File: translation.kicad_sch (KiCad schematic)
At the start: 12 parts, among them Q1 DMG1012UW-7, Q2 DMG1013UW-7, Q3 DMG1012UW-7, U4 FXLA108BQX

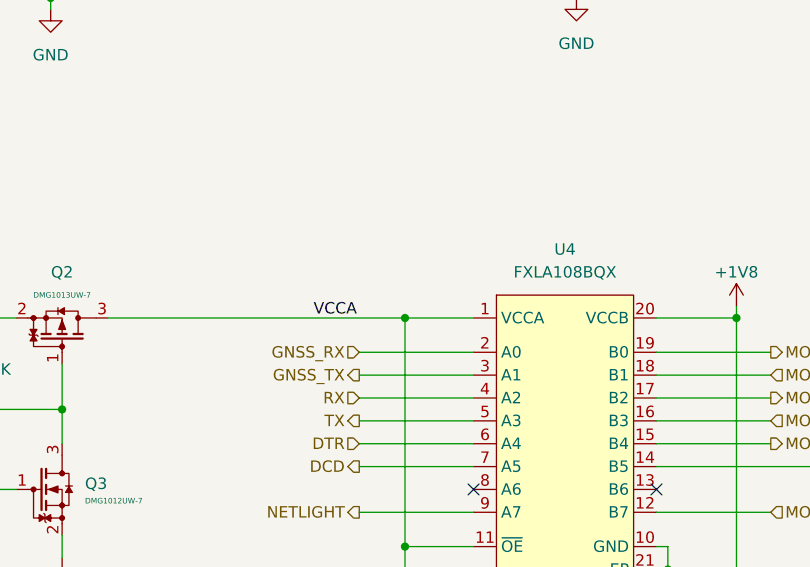
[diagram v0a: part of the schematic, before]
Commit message: Add TP for VDDA
Change board color to blue
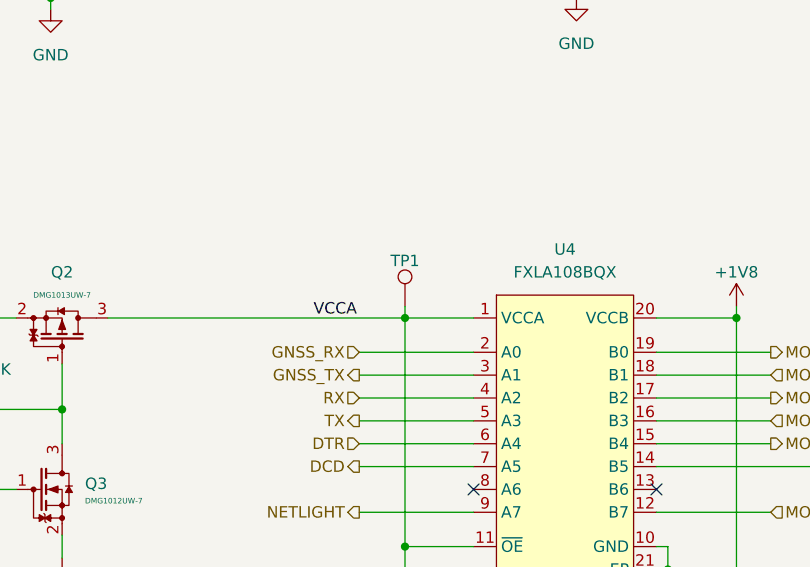
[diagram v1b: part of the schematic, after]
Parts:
- added TP1: ~, N_NonPart:TestPoint_1mm, symbol N_NonPart:TestPoint_1mm
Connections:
- net VCCA: now also TP1.1
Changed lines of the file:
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@@
+    (stroke (width 0) (type default))
+  )
+  (wire (pts (xy 120.65 91.44) (xy 120.65 92.71))
     (stroke (width 0) (type default))
   )
@@
         )
       )
+    )
+  )
+  (symbol (lib_id "N_NonPart:TestPoint_1mm") (at 120.65 91.44 0) (unit 1)
+    (in_bom no) (on_board yes) (dnp no)
+    (property "Reference" "TP1" (at 120.65 86.36 0)
+      (effects (font (size 1.27 1.27)))
+    )
+    (property "Value" "~" (at 120.65 91.44 0)
+      (effects (font (size 1.27 1.27)))
+    )
+    (property "Footprint" "N_NonPart:TestPoint_1mm" (at 120.65 91.44 0)
+      (effects (font (size 1.27 1.27)) hide)
+    )
+    (property "Datasheet" "" (at 120.65 91.44 0)
+      (effects (font (size 1.27 1.27)) hide)
+    )
+    (pin "1")
+    (instances
+      (project "Winglet-BG95"
+        (path "/332623d6-c22a-48da-966b-0d541566aa2d/8e359055-7cfc-4b97-a20a-120bbd795961"
+          (reference "TP1") (unit 1)
+        )
+        (path "/332623d6-c22a-48da-966b-0d541566aa2d/8db25416-284f-4798-9948-d4496aafbc9d"
+          (reference "TP2") (unit 1)
+        )
+      )

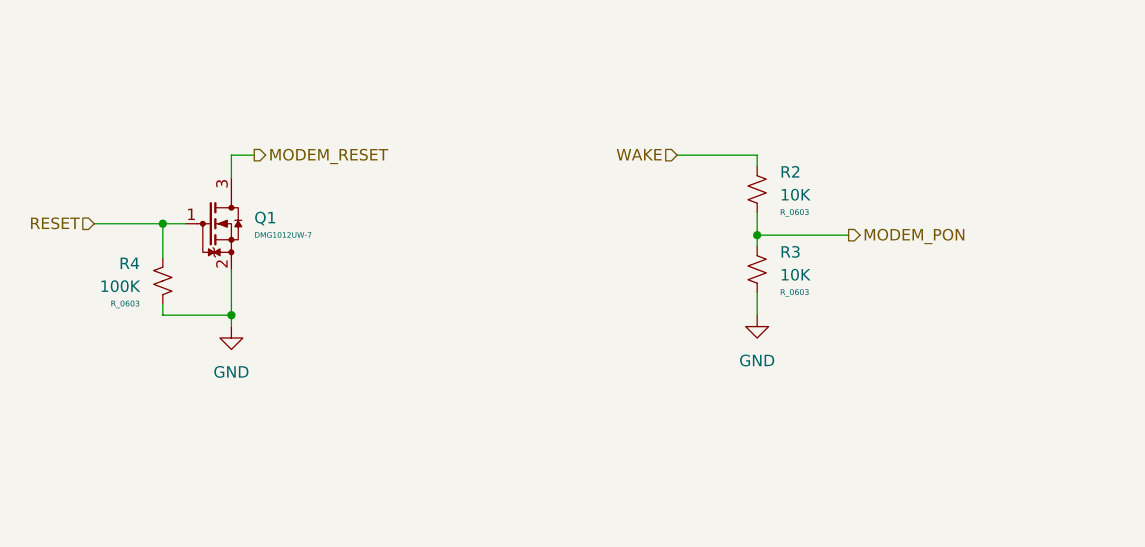
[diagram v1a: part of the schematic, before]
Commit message: Remove PON_TRIG key, add PWRKEY control.
Remove USIM options on PCIE interface.
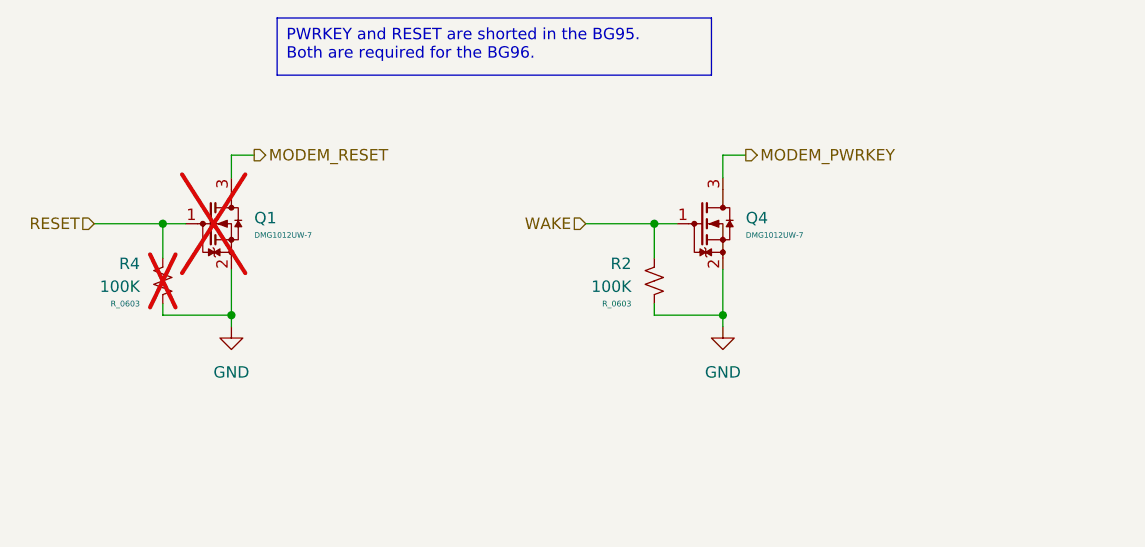
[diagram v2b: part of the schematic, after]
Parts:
- removed R3: 10K, R_Resistor:R_0603, symbol R_Resistor:R_0603
- added Q4: DMG1012UW-7, U_IC:SC70-3, symbol Q_MOSFET:DMG1012UW-7
- Q1, R4: now not fitted
- R2: value 10K -> 100K
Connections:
- net MODEM_PON is gone; now on net GND: R2.2
- net GND: now also Q4.2 (S)
- net WAKE: now also Q4.1 (G)
- new net MODEM_PWRKEY: Q4.3 (D)

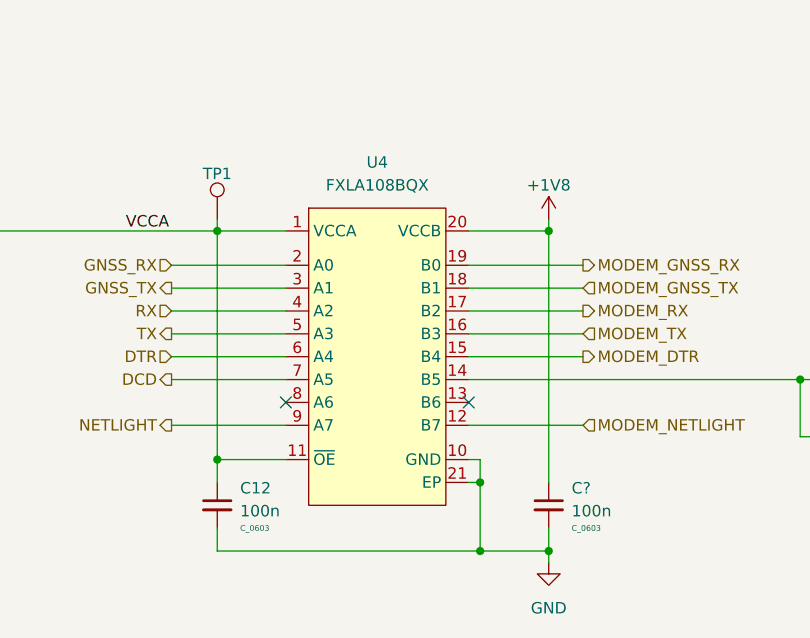
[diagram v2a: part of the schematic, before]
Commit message: Added tooling holes
Updated the readme
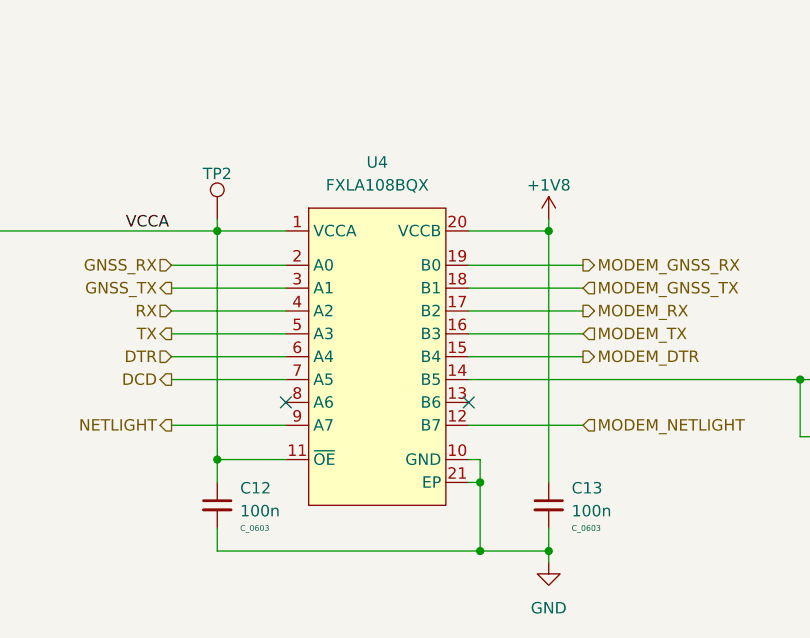
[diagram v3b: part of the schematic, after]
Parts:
- gave numbers to parts that had none: 1
- renumbered TP1 to TP2

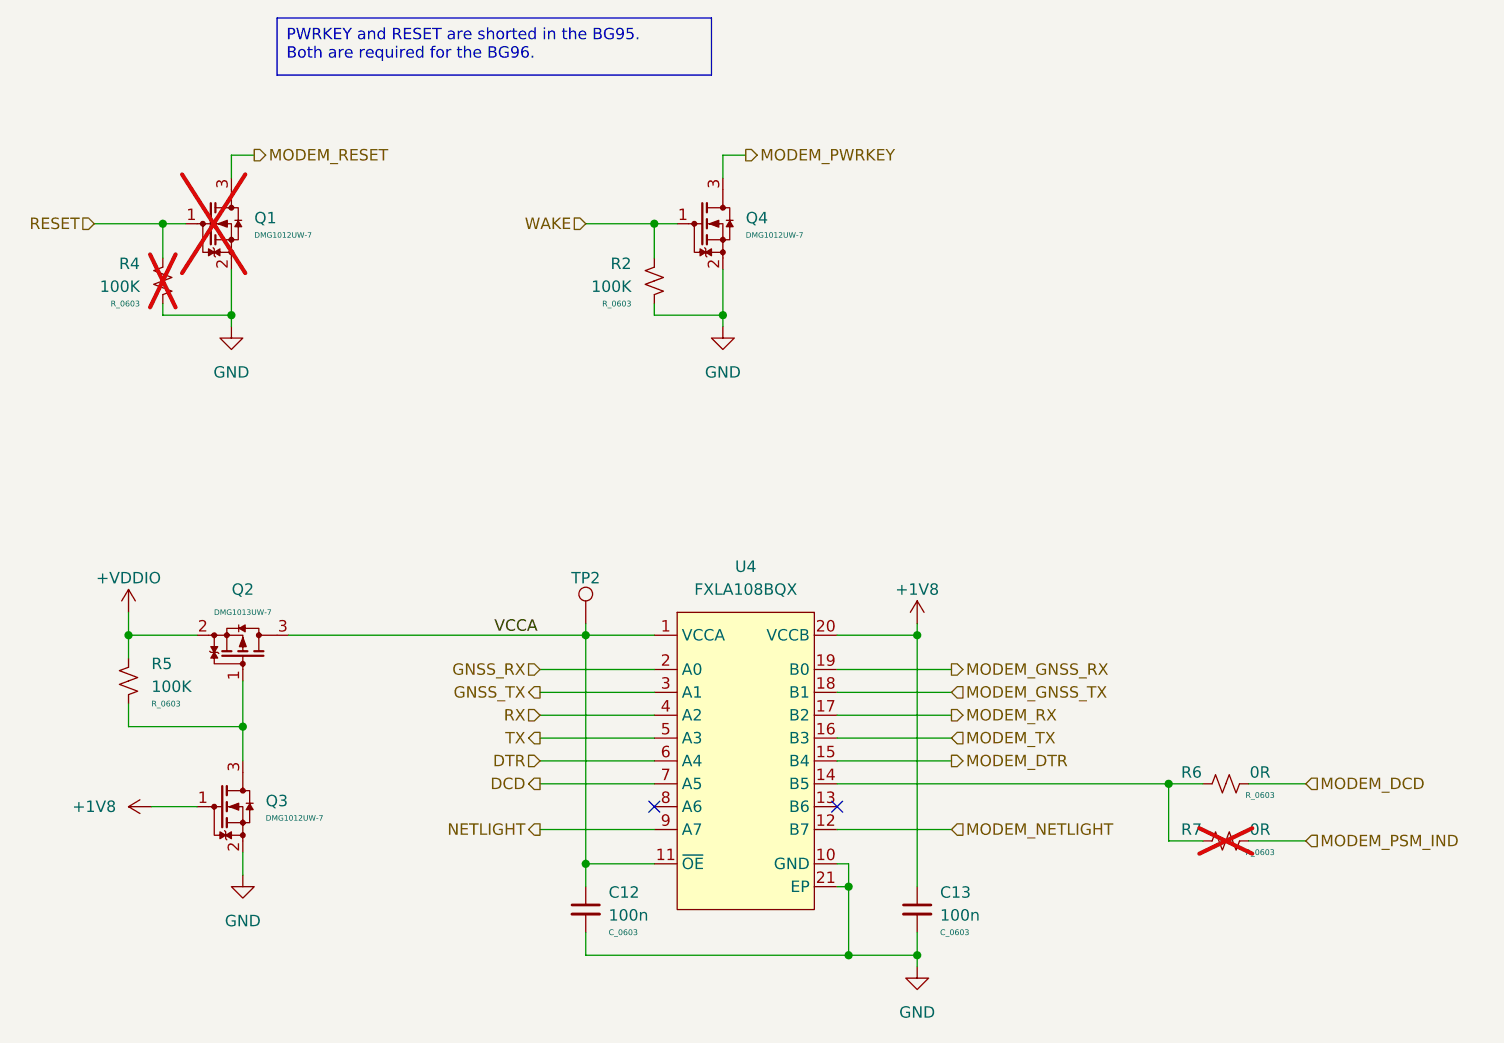
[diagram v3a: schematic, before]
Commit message: Implement fixes
Closes #2
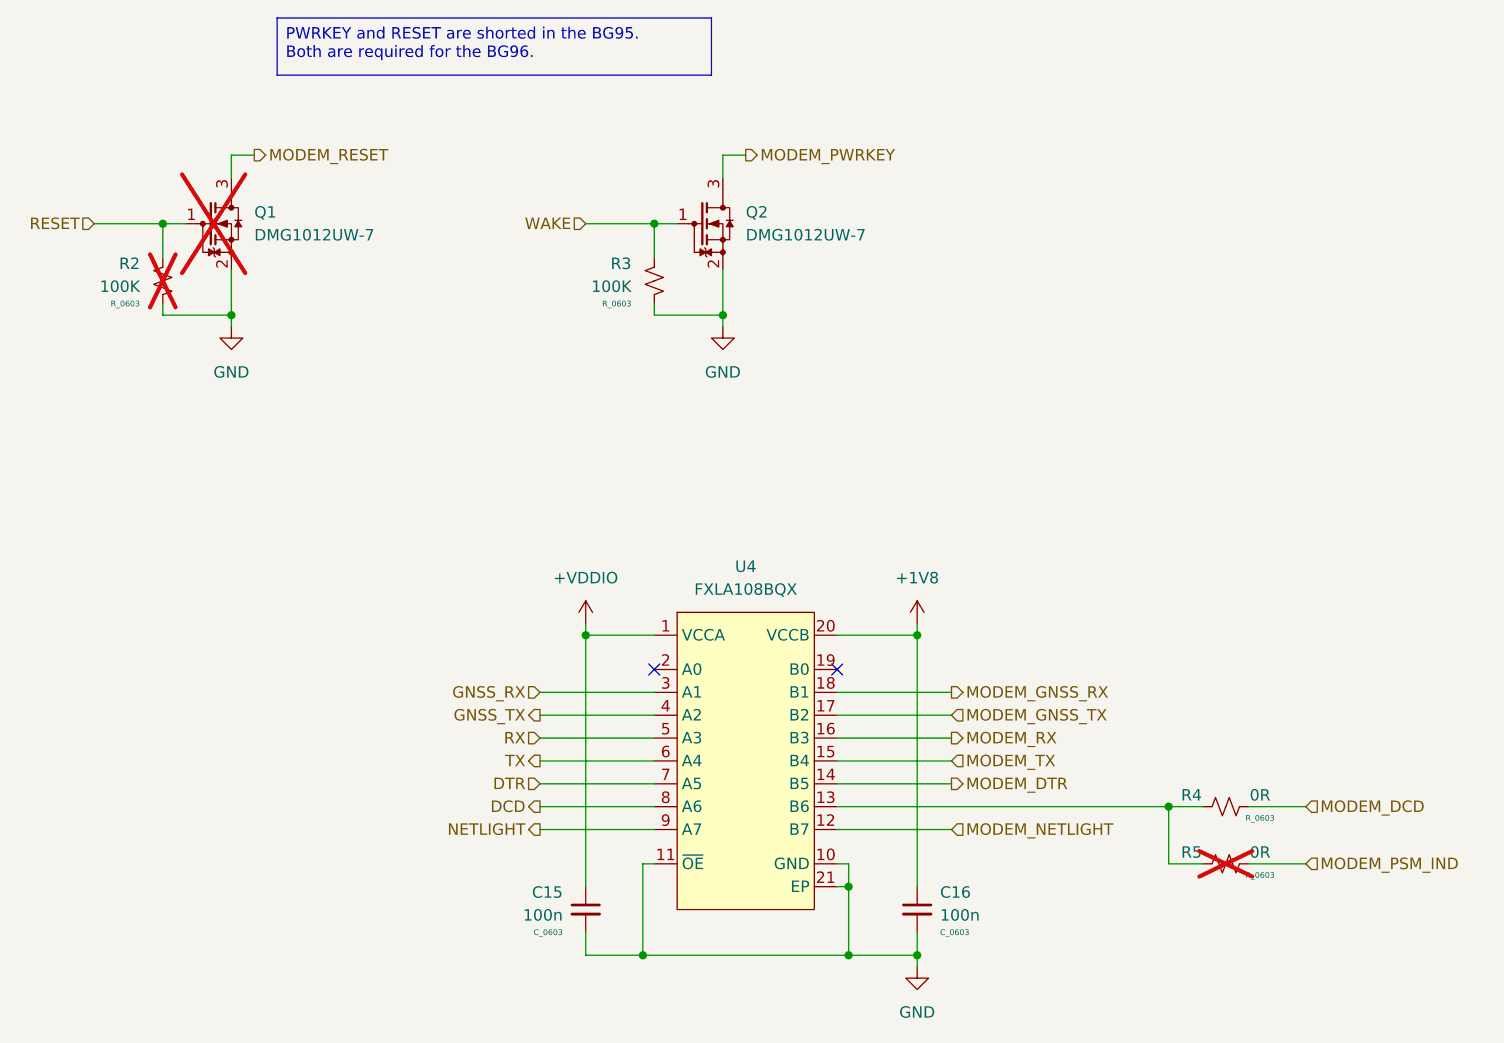
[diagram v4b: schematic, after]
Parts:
- removed Q2: DMG1013UW-7, U_IC:SC70-3, symbol Q_MOSFET:DMG1013UW-7
- removed Q3: DMG1012UW-7, U_IC:SC70-3, symbol Q_MOSFET:DMG1012UW-7
- removed R5: 100K, R_Resistor:R_0603, symbol R_Resistor:R_0603
- removed TP2: ~, N_NonPart:TestPoint_1mm, symbol N_NonPart:TestPoint_1mm
- renumbered C12 to C15, C13 to C16, Q4 to Q2, R4 to R2, R2 to R3, R6 to R4, R7 to R5
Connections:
- net +VDDIO: now also C15.1, U4.1 (VCCA)
- net DCD: now also U4.8 (A6); no longer U4.7 (A5)
- net DTR: now also U4.7 (A5); no longer U4.6 (A4)
- net GND: now also U4.11 (~{OE})
- net GNSS_RX: now also U4.3 (A1); no longer U4.2 (A0)
- net GNSS_TX: now also U4.4 (A2); no longer U4.3 (A1)
- net MODEM_DTR: now also U4.14 (B5); no longer U4.15 (B4)
- net MODEM_GNSS_RX: now also U4.18 (B1); no longer U4.19 (B0)
- net MODEM_GNSS_TX: now also U4.17 (B2); no longer U4.18 (B1)
- net MODEM_RX: now also U4.16 (B3); no longer U4.17 (B2)
- net MODEM_TX: now also U4.15 (B4); no longer U4.16 (B3)
- net RX: now also U4.5 (A3); no longer U4.4 (A2)
- net TX: now also U4.6 (A4); no longer U4.5 (A3)
- net at R4.2, R5.2: now also U4.13 (B6); no longer U4.14 (B5)
- removed net VCCA: C15.1, U4.1 (VCCA), U4.11 (~{OE})
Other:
- company: (none) -> TL Embedded
- title: (none) -> Winglet BG95
- moved on the sheet: R4, R5

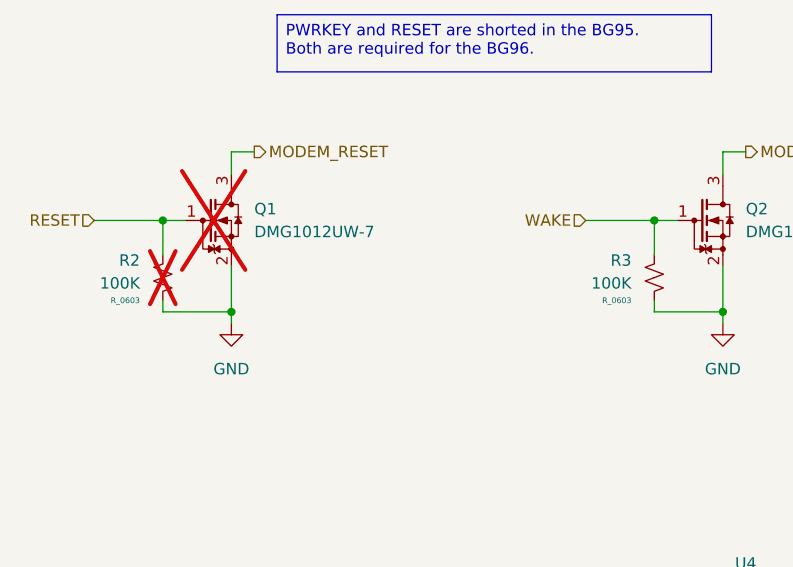
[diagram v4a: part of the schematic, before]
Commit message: Move to NSIM-16-B sim card holder for easier sourcing
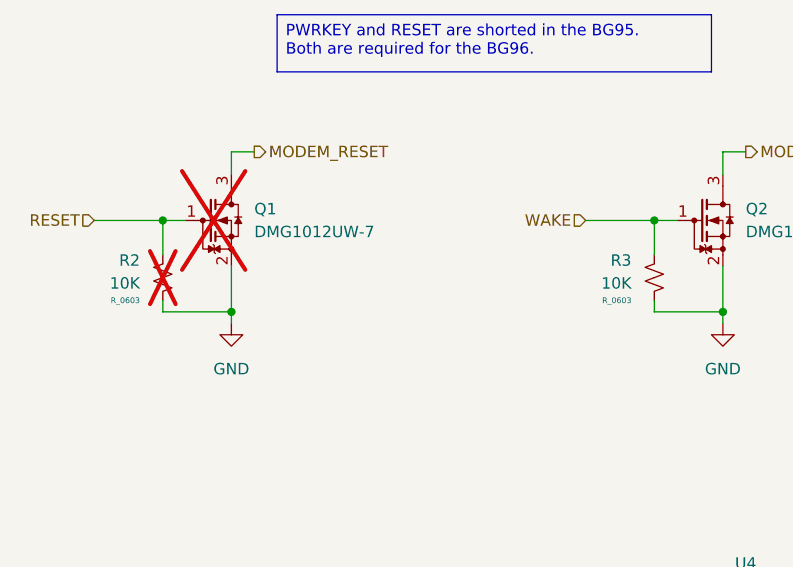
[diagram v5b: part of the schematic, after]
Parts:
- R2, R3: value 100K -> 10K
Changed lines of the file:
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@@
 			)
 		)
-		(property "Value" "100K"
+		(property "Value" "10K"
 			(at 71.12 53.975 0)
 			(effects
@@
 			)
 		)
-		(property "Value" "100K"
+		(property "Value" "10K"
 			(at 125.73 53.975 0)
 			(effects
